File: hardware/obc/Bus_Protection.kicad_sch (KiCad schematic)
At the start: 35 parts, among them Q201 BSS138PS,115, Q202 BSS138PS,115, Q203 MBT2222ADW1T1, Q204 MBT2222ADW1T1, Q205 BSS138PS,115, Q206 BSS138PS,115, Q207 MBT2222ADW1T1, Q208 MBT2222ADW1T1

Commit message: obc: Fixed errors from design review
- Gave proper attribution on all pages
- Spread out components on Avionics page
- Changed GPS power circuit
- Added a DNP resistor in between VBATT and VWATCHEDRAIL
- Added various other part numbers on Power Supervisor and Watch Dog Page
- Changed Power Supervisor and Watch Dog Page to page 3
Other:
- company: Ruchir Kavulli, Michael Lyle -> Ruchir Kavulli, Luke Titi, Michael Lyle
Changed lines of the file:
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@@
 		(date "2024-06-07")
 		(rev "1")
-		(company "Ruchir Kavulli, Michael Lyle")
+		(company "Ruchir Kavulli, Luke Titi, Michael Lyle")
 		(comment 1 "Derived from PyCubed Mainboard v5")
 	)

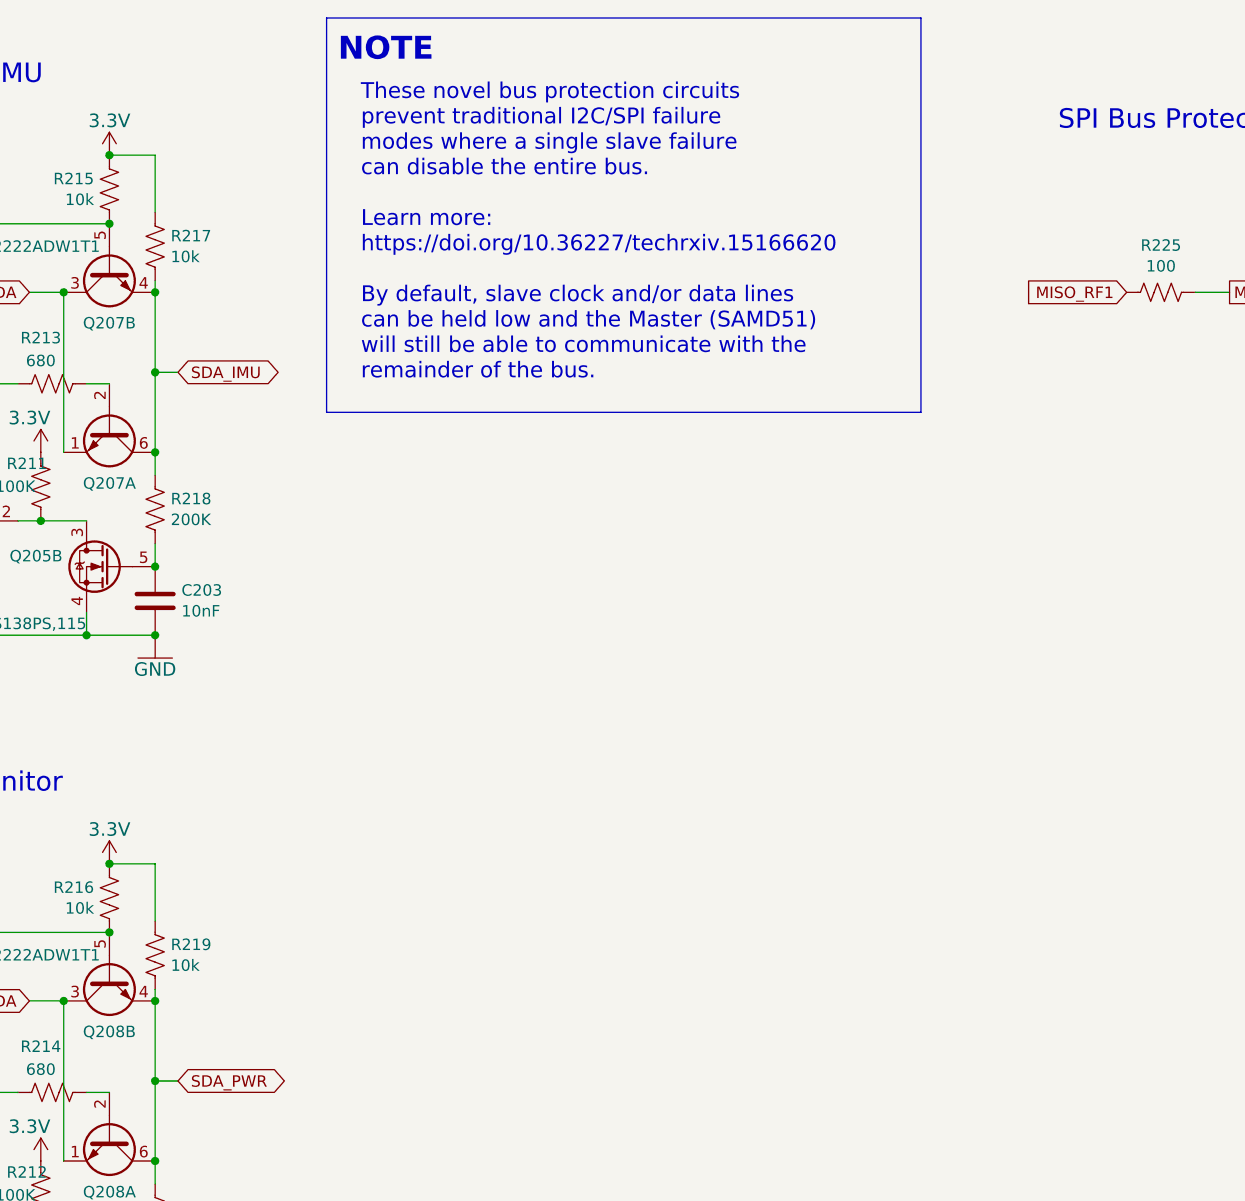
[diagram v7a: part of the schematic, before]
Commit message: obc: Fixed second design review, and fixed up BOM
- added layout comments on schematic
- fixed various comments
- added many LCSC # for components
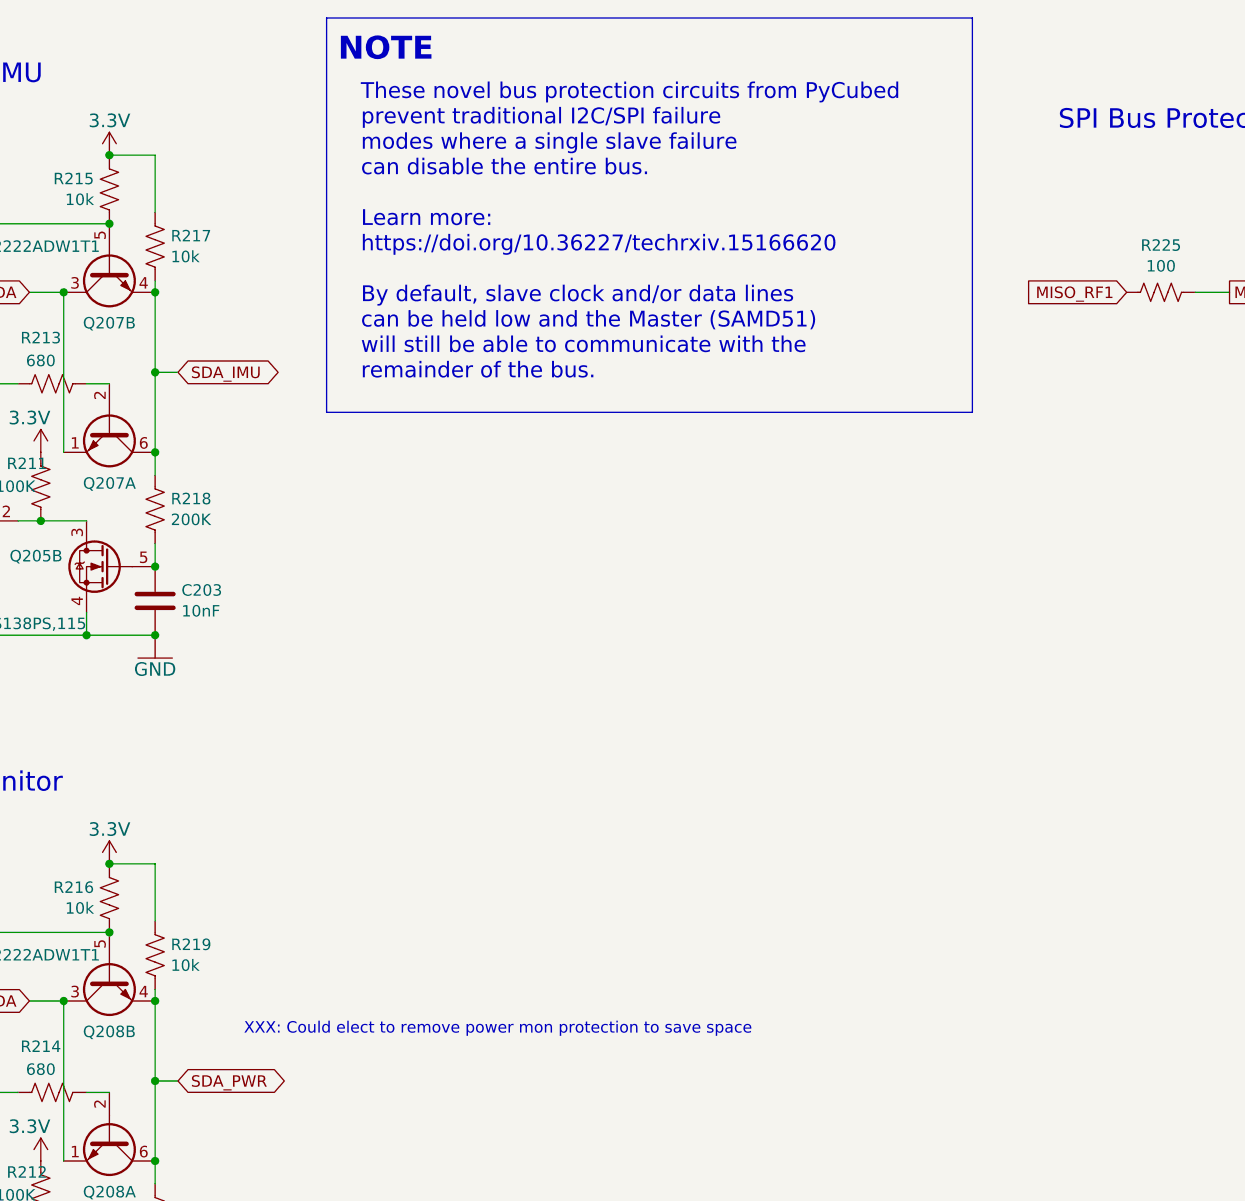
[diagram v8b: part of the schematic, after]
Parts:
- R225, R227, R228: LCSC (none) -> C105588
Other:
- note added: "These novel bus protection circuits from PyCubed prevent traditional I2C/SPI failure modes where a single slave failure can disable the entire bus. Learn more: https://doi.org/10.36227/techrxiv.15166620 By default, slave clock and/or data lines can be held low and the Master (SAMD51) will still be able to communicate with the remainder of the bus."
- note added: "XXX: Could elect to remove power mon protection to save space"
- note removed: "These novel bus protection circuits prevent traditional I2C/SPI failure modes where a single slave failure can disable the entire bus. Learn more: https://doi.org/10.36227/techrxiv.15166620 By default, slave clock and/or data lines can be held low and the Master (SAMD51) will still be able to communicate with the remainder of the bus."
